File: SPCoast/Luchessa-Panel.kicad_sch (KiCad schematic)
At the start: 21 parts, among them SW8784 783, SW8796 795, SW8800 799, U8004 0x24, U8005 0x25, U8006 0x26

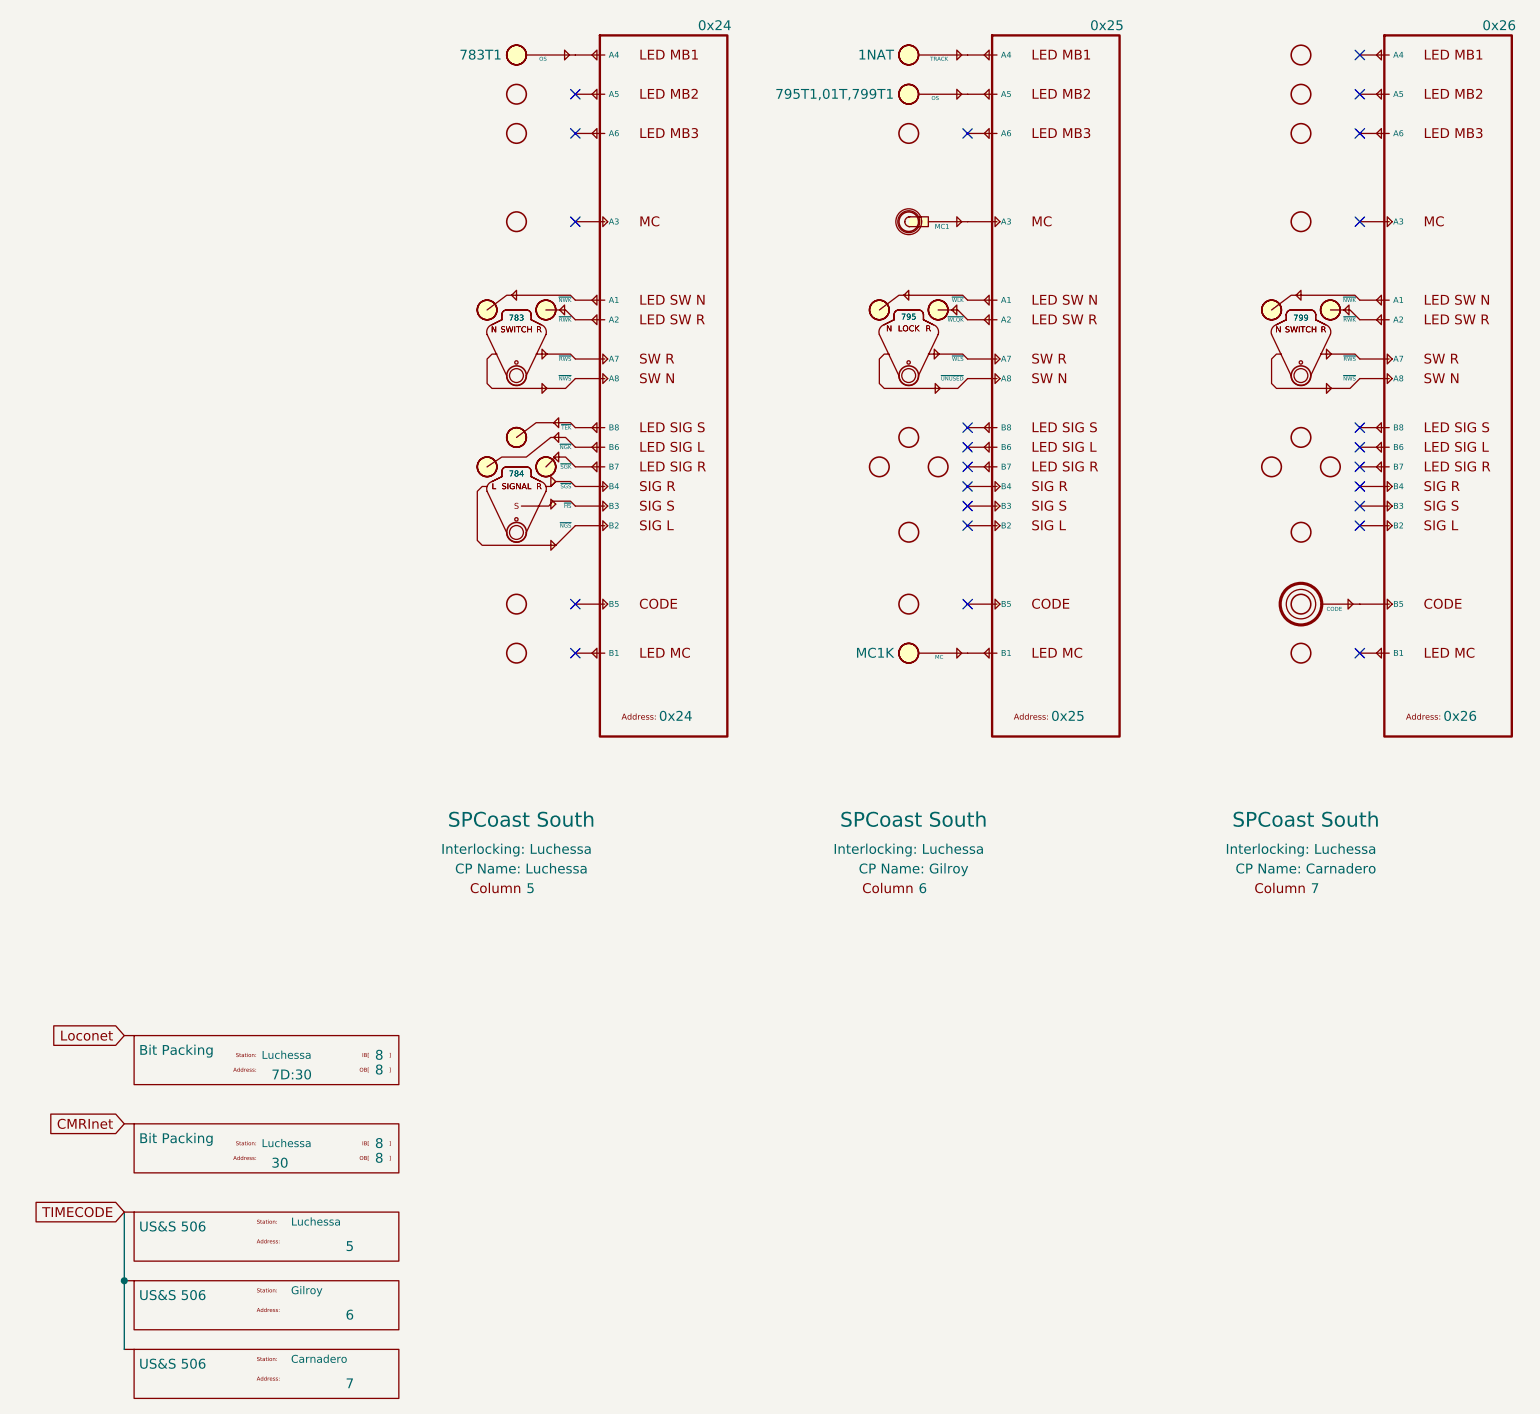
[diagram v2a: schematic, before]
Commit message: feat(kicad): deployment cases: Caltrain on a CMRInet node, Gilroy Interchange JMRI turnouts over MQTT
Gilroy Caltrain: field I/O drawn as per-bit CMRInet drivers (Driver-CMRI-IB/OB,
UA 30, 14 in / 20 out) with named devices for 3 switches, 5 track circuits and
7 heads (four encoder-wired, three lamp-wired). No processor is named: every
chip is on the hosted CMRInet bus, so the field unit runs on that bus's host.

Gilroy Interchange: proof of concept for JMRI turnouts and sensors over MQTT
(Driver-JMRI-Turnout, -Turnout-Feedback, -Sensor-Feedback) on switches 777
and 781. Known: the 777 drivers carry Address 771 (typo, fixed by the
follow-up rewrite); the JMRI symbols fail lint_symbol_fields (Pin.D names no
pin, Topic/States casing), also fixed by the rewrite.

Libraries: Railroad-HardwareIO gains Driver-CMRI-IB/OB and the four JMRI
drivers; Railroad-Field's Device-Head-CPL pins renumbered top down (G, Y, R).
Nine other sheets were re-saved by KiCad with property placements only.

Verified:
- kicad-cli ERC: 0 violations, whole project
- every Caltrain and Gilroy Interchange device binds; no duplicate CMRI bits
- netlist_diff vs post-sync.net: only additions on the two sheets (49 parts,
  34 nets, 68 nodes), nothing lost or changed elsewhere
- library-owned field drift on the new instances: 0

Co-Authored-By: Claude Fable 5.1 <noreply@anthropic.com>
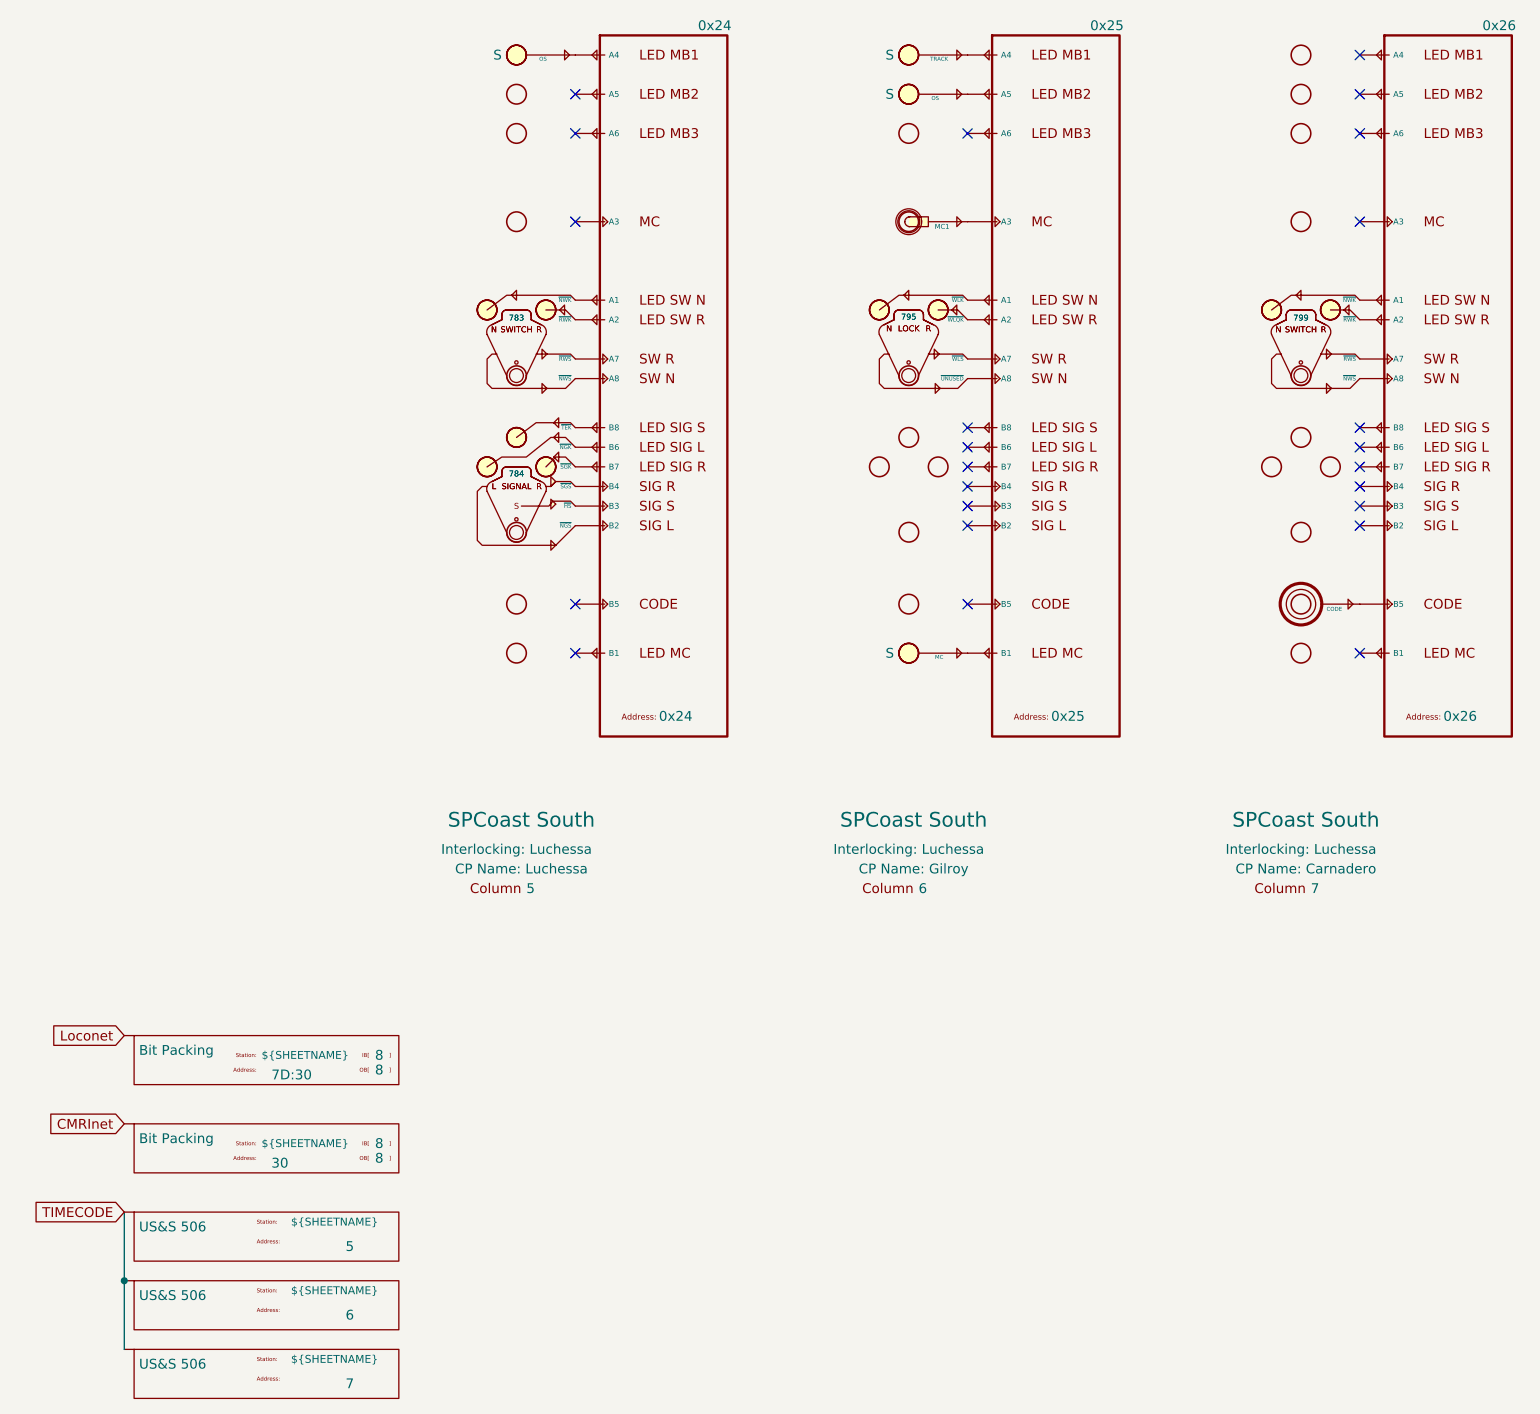
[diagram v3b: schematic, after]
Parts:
- Encoding8002, Encoding8005, Encoding8006: Station Luchessa -> ${SHEETNAME}
- Encoding8003: Station Gilroy -> ${SHEETNAME}
- Encoding8004: Station Carnadero -> ${SHEETNAME}
- LAMP8005: IndicationToken 783T1 -> S
- LAMP8006: IndicationToken 1NAT -> S
- LAMP8007: IndicationToken 795T1,01T,799T1 -> S
- LAMP8008: IndicationToken MC1K -> S
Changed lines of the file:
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@@
 			)
 		)
-		(property "ki_locked" ""
-			(at 80.01 83.82 0)
-			(hide yes)
-			(show_name no)
-			(do_not_autoplace no)
-			(effects
-				(font
-					(size 1.27 1.27)
-				)
-			)
-		)
 		(pin "5"
 		)
@@
 			)
 		)
-		(property "ki_locked" ""
-			(at 80.01 63.5 0)
-			(hide yes)
-			(show_name no)
-			(do_not_autoplace no)
-			(effects
-				(font
-					(size 1.27 1.27)
-				)
-			)
-		)
 		(pin "4"
 		)
@@
 			)
 		)
-		(property "Station" "Gilroy"
+		(property "Station" "${SHEETNAME}"
 			(at 50.8 186.69 0)
 			(show_name no)
@@
 			)
 		)
-		(property "IndicationToken" "MC1K"
+		(property "IndicationToken" "S"
 			(at 128.905 104.14 0)
 			(show_name no)
@@
 			)
 		)
-		(property "ki_locked" ""
-			(at 130.81 63.5 0)
-			(hide yes)
-			(show_name no)
-			(do_not_autoplace no)
-			(effects
-				(font
-					(size 1.27 1.27)
-				)
-			)
-		)
 		(pin "1"
 		)
@@
 			)
 		)
-		(property "IndicationToken" "783T1"
+		(property "IndicationToken" "S"
 			(at 78.105 26.67 0)
 			(show_name no)
@@
 			)
 		)
-		(property "ki_locked" ""
-			(at 80.01 63.5 0)
-			(hide yes)
-			(show_name no)
-			(do_not_autoplace no)
-			(effects
-				(font
-					(size 1.27 1.27)
-				)
-			)
-		)
 		(pin "1"
 		)
@@
 			)
 		)
-		(property "Station" "Luchessa"
+		(property "Station" "${SHEETNAME}"
 			(at 46.99 167.64 0)
 			(show_name no)
@@
 			)
 		)
-		(property "Station" "Luchessa"
+		(property "Station" "${SHEETNAME}"
 			(at 50.8 177.8 0)
 			(show_name no)
@@
 			)
 		)
-		(property "IndicationToken" "1NAT"
+		(property "IndicationToken" "S"
 			(at 128.905 26.67 0)
 			(show_name no)
@@
 			)
 		)
-		(property "ki_locked" ""
-			(at 130.81 63.5 0)
-			(hide yes)
-			(show_name no)
-			(do_not_autoplace no)
-			(effects
-				(font
-					(size 1.27 1.27)
-				)
-			)
-		)
 		(pin "4"
 		)
@@
 			)
 		)
-		(property "ki_locked" ""
-			(at 181.61 63.5 0)
-			(hide yes)
-			(show_name no)
-			(do_not_autoplace no)
-			(effects
-				(font
-					(size 1.27 1.27)
-				)
-			)
-		)
 		(pin "1"
 		)
@@
 			)
 		)
-		(property "IndicationToken" "795T1,01T,799T1"
+		(property "IndicationToken" "S"
 			(at 128.905 31.75 0)
 			(show_name no)
@@
 			)
 		)
-		(property "ki_locked" ""
-			(at 80.01 83.82 0)
-			(hide yes)
-			(show_name no)
-			(do_not_autoplace no)
-			(effects
-				(font
-					(size 1.27 1.27)
-				)
-			)
-		)
 		(pin "1"
 		)
@@
 			)
 		)
-		(property "Station" "Carnadero"
+		(property "Station" "${SHEETNAME}"
 			(at 50.8 195.58 0)
 			(show_name no)
@@
 			)
 		)
-		(property "ki_locked" ""
-			(at 181.61 63.5 0)
-			(hide yes)
-			(show_name no)
-			(do_not_autoplace no)
-			(effects
-				(font
-					(size 1.27 1.27)
-				)
-			)
-		)
 		(pin "4"
 		)
@@
 			)
 		)
-		(property "Station" "Luchessa"
+		(property "Station" "${SHEETNAME}"
 			(at 46.99 156.21 0)
 			(show_name no)
